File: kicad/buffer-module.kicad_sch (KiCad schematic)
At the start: 10 parts, among them J1 Jack_InA, J2 Jack_InB, J3 Jack_OutA-1, J4 Jack_OutA-2, J5 Jack_OutA-3, J6 Jack_OutB-1, J7 Jack_OutB-2, J8 Jack_OutB-3

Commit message: Refactor buffer-module: Remove unused silk layers and update footprint references
- Removed multiple unused silk layer entries from buffer-module.kicad_pro to clean up the design.
- Updated footprint references in buffer-module.kicad_sch from "AudioJacks2" to "Eurorack" for consistency across the schematic.
- Deleted the lock file ~buffer-module.kicad_sch.lck as it is no longer needed.
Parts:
- J1, J2, J3, J4, J5, J6, J7, J8: footprint AudioJacks2:Jack_3.5mm_QingPu_WQP-PJ398SM_Vertical -> Eurorack:Jack_3.5mm_QingPu_WQP-PJ398SM_Vertical
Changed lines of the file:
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@@
 			)
 		)
-		(property "Footprint" "AudioJacks2:Jack_3.5mm_QingPu_WQP-PJ398SM_Vertical"
+		(property "Footprint" "Eurorack:Jack_3.5mm_QingPu_WQP-PJ398SM_Vertical"
 			(at 248.92 82.55 0)
 			(effects
@@
 			)
 		)
-		(property "Footprint" "AudioJacks2:Jack_3.5mm_QingPu_WQP-PJ398SM_Vertical"
+		(property "Footprint" "Eurorack:Jack_3.5mm_QingPu_WQP-PJ398SM_Vertical"
 			(at 248.92 67.31 0)
 			(effects
@@
 			)
 		)
-		(property "Footprint" "AudioJacks2:Jack_3.5mm_QingPu_WQP-PJ398SM_Vertical"
+		(property "Footprint" "Eurorack:Jack_3.5mm_QingPu_WQP-PJ398SM_Vertical"
 			(at 177.8 67.31 0)
 			(effects
@@
 			)
 		)
-		(property "Footprint" "AudioJacks2:Jack_3.5mm_QingPu_WQP-PJ398SM_Vertical"
+		(property "Footprint" "Eurorack:Jack_3.5mm_QingPu_WQP-PJ398SM_Vertical"
 			(at 115.57 82.55 0)
 			(effects
@@
 			)
 		)
-		(property "Footprint" "AudioJacks2:Jack_3.5mm_QingPu_WQP-PJ398SM_Vertical"
+		(property "Footprint" "Eurorack:Jack_3.5mm_QingPu_WQP-PJ398SM_Vertical"
 			(at 115.57 97.79 0)
 			(effects
@@
 			)
 		)
-		(property "Footprint" "AudioJacks2:Jack_3.5mm_QingPu_WQP-PJ398SM_Vertical"
+		(property "Footprint" "Eurorack:Jack_3.5mm_QingPu_WQP-PJ398SM_Vertical"
 			(at 248.92 97.79 0)
 			(effects
@@
 			)
 		)
-		(property "Footprint" "AudioJacks2:Jack_3.5mm_QingPu_WQP-PJ398SM_Vertical"
+		(property "Footprint" "Eurorack:Jack_3.5mm_QingPu_WQP-PJ398SM_Vertical"
 			(at 44.45 67.31 0)
 			(effects
@@
 			)
 		)
-		(property "Footprint" "AudioJacks2:Jack_3.5mm_QingPu_WQP-PJ398SM_Vertical"
+		(property "Footprint" "Eurorack:Jack_3.5mm_QingPu_WQP-PJ398SM_Vertical"
 			(at 115.57 67.31 0)
 			(effects

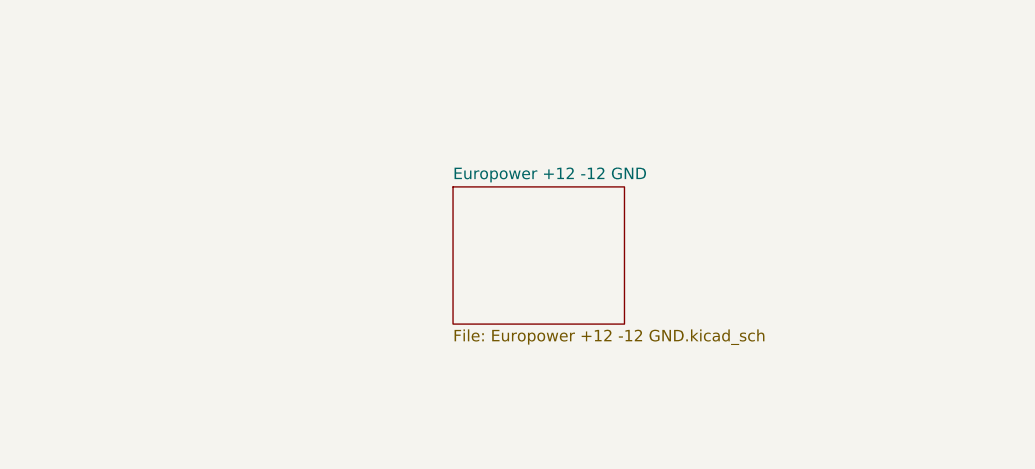
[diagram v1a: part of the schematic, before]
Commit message: Refactor KiCad project files for improved layout and organization
- Adjusted column widths in buffer-module.kicad_prl for better readability.
- Cleared unnecessary DRC exclusions in buffer-module.kicad_pro to streamline design rules.
- Updated sheet positions and properties in buffer-module.kicad_sch for enhanced clarity.
- Realigned junctions and wires in quad buffer schematic for improved circuit flow and readability.
- Corrected component positions and properties in quad buffer schematic to ensure accurate representation.
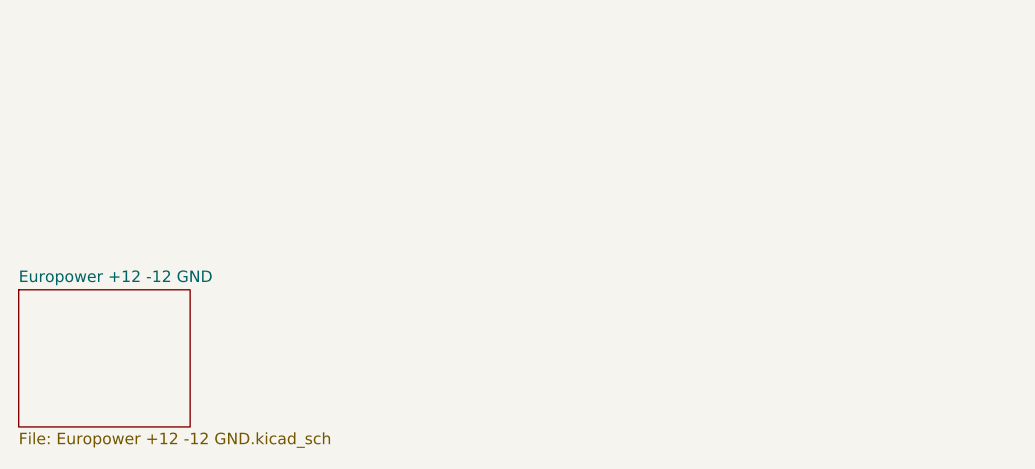
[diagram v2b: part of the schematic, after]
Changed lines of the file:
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@@
 	)
 	(sheet
-		(at 77.47 156.21)
+		(at 29.21 167.64)
 		(size 19.05 15.24)
 		(exclude_from_sim no)
@@
 		)
 		(property "Sheetname" "Europower +12 -12 GND"
-			(at 77.47 155.4984 0)
+			(at 29.21 166.9284 0)
 			(effects
 				(font
@@
 		)
 		(property "Sheetfile" "Europower +12 -12 GND.kicad_sch"
-			(at 77.47 172.0346 0)
+			(at 29.21 183.4646 0)
 			(effects
 				(font
